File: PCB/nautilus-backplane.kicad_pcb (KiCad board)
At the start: 4 copper layers, 180 x 60 mm, 96 parts, among them J1 DE9_Socket_MountingHoles, J18 615008138321, J7 643280100305, J8 EdgeConn_Full, J9 643280100305

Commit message: Traced ethernet
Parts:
- moved TP1 50.8 mm to (269.5, 115.2)
- moved TP2 50.8 mm to (267.0, 115.2)
- moved JP15 41.6 mm to (173.6, 90.1)
- moved JP16 41.6 mm to (170.4, 90.1)
- moved JP17 41.6 mm to (173.6, 92.6)
- moved JP18 41.6 mm to (170.3, 92.6)
- moved JP27 41.6 mm to (162.8, 99.1)
- moved JP28 41.6 mm to (162.8, 94.1)
- moved JP29 41.6 mm to (162.8, 96.6)
- moved TP3 34.0 mm to (259.6, 110.7)
- moved J1 29.3 mm to (259.5, 77.2)
- moved J18 18.6 mm to (225.6, 102.5), turned to 90 degrees
- moved JP8 17.1 mm to (216.1, 110.6), turned to 0 degrees
- moved JP6 14.9 mm to (219.6, 109.4), turned to 0 degrees
- moved JP7 13.9 mm to (219.6, 111.9), turned to 0 degrees
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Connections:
- net /A16 renamed e1_3+
- net /A17 renamed e1_3-
- net /A18 renamed e1_2-
- net /A19 renamed e1_2+
- net /B12 renamed e2_1+
- net /B13 renamed e2_1-
- net /B14 renamed e2_0-
- net /B15 renamed e2_0+
- net /B16 renamed e1_1+
- net /B17 renamed e1_1-
- net /B18 renamed e1_0-
- net /B19 renamed e1_0+
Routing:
- net e1_0+: track 0.00 -> 64.8 mm
- net e1_0-: track 0.00 -> 64.5 mm
- net e1_1+: track 0.00 -> 63.1 mm
- net e1_1-: track 0.00 -> 63.1 mm
- net e1_2+: track 0.00 -> 59.2 mm
- net e1_2-: track 0.00 -> 59.0 mm
- net /TRD0.D+: track 22.6 -> 74.1 mm
- net /TRD0.D-: track 22.7 -> 74.1 mm
- net e1_3+: track 0.00 -> 48.0 mm
- net e1_3-: track 0.00 -> 47.7 mm
- net /TRD1.D+: track 22.6 -> 67.1 mm
- net /TRD1.D-: track 22.7 -> 67.1 mm
- net e2_0+: track 0.00 -> 24.4 mm
- net e2_0-: track 0.00 -> 24.4 mm
- net e2_1-: track 0.00 -> 20.6 mm
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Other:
- board text added: "24V"

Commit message: placed banana connectors for power
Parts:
- removed J7: 643280100305, dz_con:Wuerth_WR_CIRCM_643280100305
- added J2: 24.245.2, dz_con:ANT-TH_L33.0-W12.0, F.Cu at (118.5, 102.4)
- added J3: 24.245.2, dz_con:ANT-TH_L33.0-W12.0, F.Cu at (118.4, 122.0)
- added J4: 24.245.2, dz_con:ANT-TH_L33.0-W12.0, F.Cu at (118.5, 82.9)
- added J5: 24.245.2, dz_con:ANT-TH_L33.0-W12.0, F.Cu at (225.9, 80.7)
- moved TP1 152.4 mm to (117.1, 114.1), turned to -90 degrees
- moved TP2 151.3 mm to (117.1, 94.5), turned to -90 degrees
- moved J1 71.5 mm to (188.1, 81.4), turned to 180 degrees
- moved TP4 64.5 mm to (117.1, 74.9)
- moved TP3 40.6 mm to (233.7, 79.4)
- moved JP15 20.1 mm to (193.7, 90.8)
- moved JP16 20.1 mm to (190.5, 90.8)
- moved JP17 20.1 mm to (193.7, 93.3)
- moved JP18 20.1 mm to (190.4, 93.3)
- moved JP53 19.4 mm to (156.9, 104.8)
- moved JP54 19.4 mm to (156.9, 102.3)
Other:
- board size 180 x 60 mm -> 130.2 x 60.1 mm
- board text added: "3V3"
- board text added: "3v3"
- board text added: "5V"
- board text added: "GND"
- board text removed: "MB & CU"

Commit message: Traced CAN
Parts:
- JP15, JP16, JP17, JP18, JP27, JP28, JP29: moved to F.Cu
- JP35, JP36, JP50, JP51, JP52, R5, TP33, TP34: moved to B.Cu
- moved J9 225.1 mm to (163.9, 78.7), turned to 180 degrees
- moved JP50 146.3 mm to (192.8, 87.7), turned to 90 degrees
- moved TP33 146.2 mm to (206.5, 85.0), turned to -90 degrees
- moved TP34 146.0 mm to (206.5, 87.5), turned to -90 degrees
- moved JP52 145.2 mm to (190.3, 87.7), turned to 90 degrees
- moved R5 141.9 mm to (209.8, 87.6), turned to 180 degrees
- moved JP51 138.4 mm to (213.2, 85.0), turned to -90 degrees
- moved JP35 130.1 mm to (200.8, 87.7), turned to 90 degrees
- moved JP36 126.4 mm to (198.3, 87.7), turned to 90 degrees
- moved JP47 102.7 mm to (171.2, -25.7)
- moved JP48 102.7 mm to (171.2, -21.9)
- moved JP49 102.7 mm to (171.2, -18.1)
- moved JP43 102.7 mm to (165.9, -43.1)
- moved JP44 102.7 mm to (165.9, -39.3)
- moved JP45 102.7 mm to (165.9, -35.4)
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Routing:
- net /FISH/CAN.H: track 0.00 -> 88.5 mm, vias 0 -> 2
- net e2_1-: track 20.6 -> 107.0 mm, vias 0 -> 2
- net /FISH/CAN.L: track 0.00 -> 72.2 mm, vias 0 -> 2
- net /A13: track 0.00 -> 67.5 mm, vias 0 -> 1
- net /A12: track 0.00 -> 59.5 mm, vias 0 -> 2
- net e2_1+: track 20.6 -> 60.5 mm, vias 0 -> 2
- net /B31: track 0.00 -> 31.3 mm
- net /B32: track 0.00 -> 31.0 mm
- net Net-(JP51-B): track 0.00 -> 2.58 mm
- net e1_2+: track 59.2 -> 57.8 mm
- net e1_2-: track 59.0 -> 57.6 mm
- net e1_3+: track 48.0 -> 46.6 mm
- net e1_3-: track 47.7 -> 46.3 mm
- net GND: vias 0 -> 8
- net +5V: vias 0 -> 4
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- added copper zone on B.Cu, net +24V
- added copper zone on In2.Cu, net +24V
- added copper zone on F.Cu, net +3V3
- added copper zone on F.Cu, net +5V
- added copper zone on B.Cu, net /B45
- added copper zone on B.Cu, net /B48
- added copper zone on In2.Cu, net GND
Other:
- board text added: "BMS"
- board text added: "CAN Term"
- board text added: "CAN_H"
- board text added: "CAN_L"

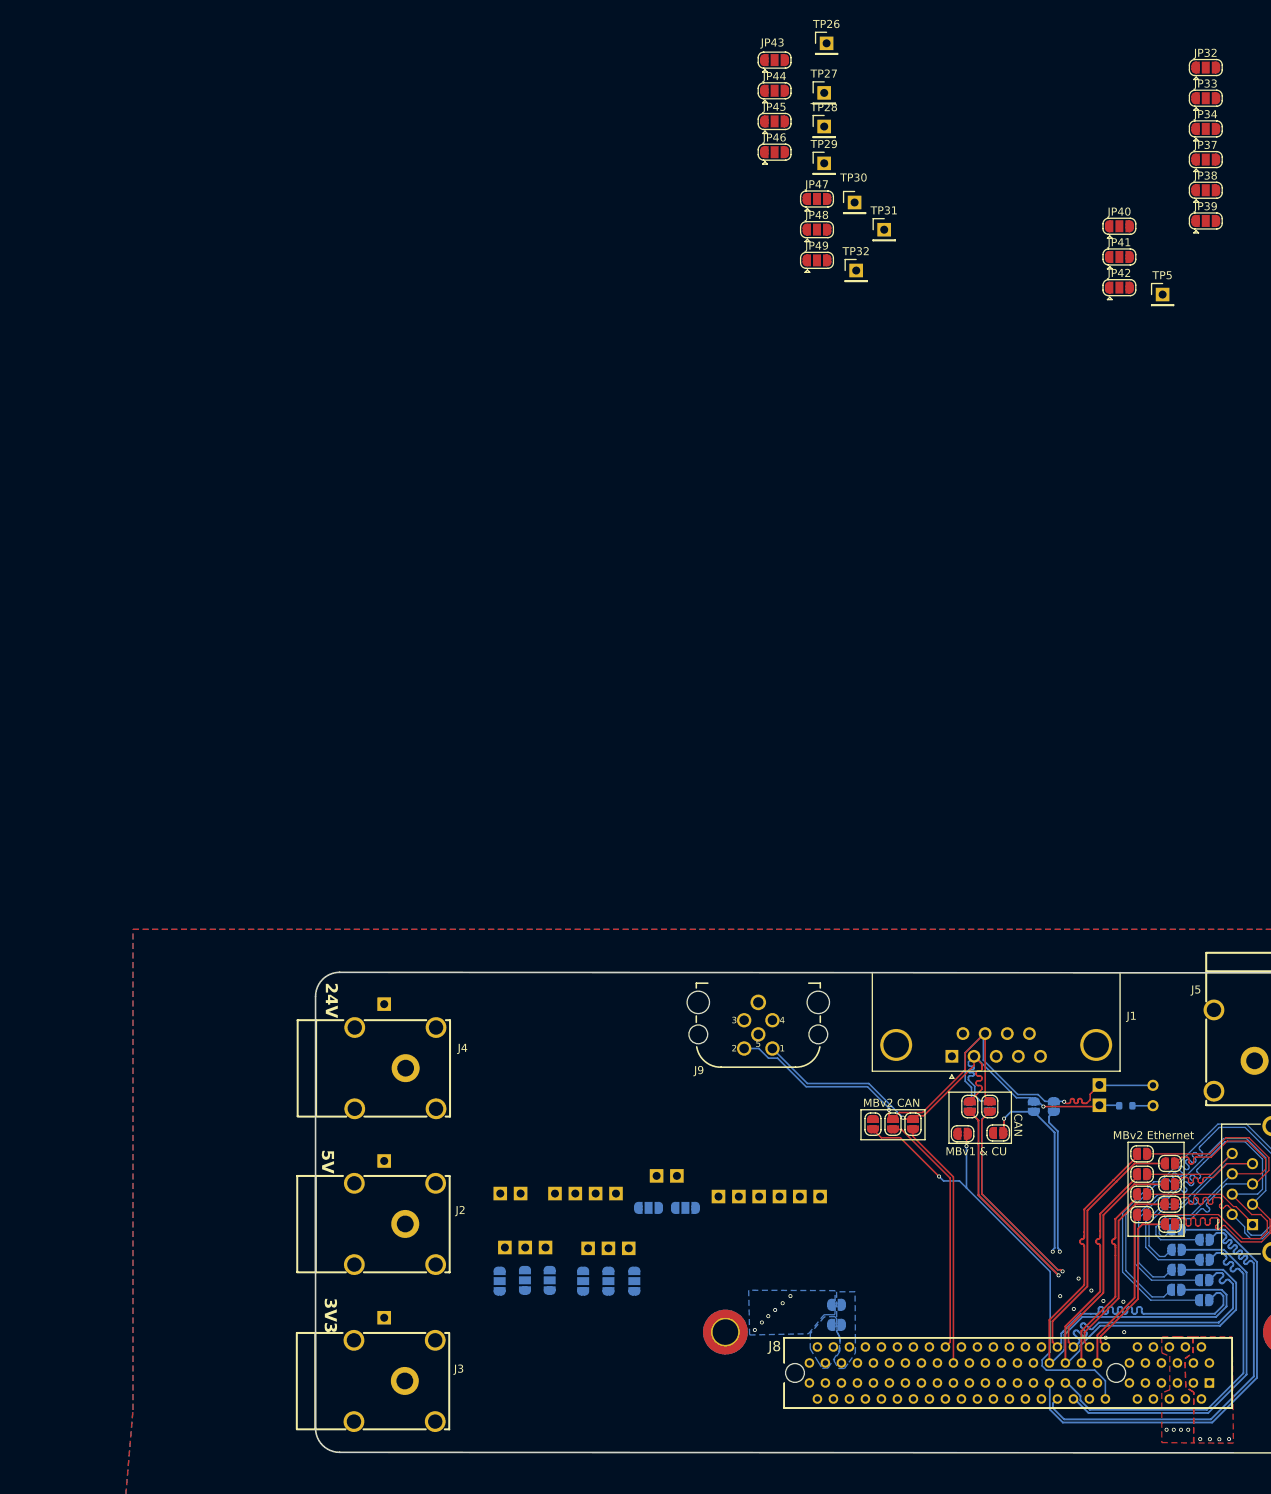
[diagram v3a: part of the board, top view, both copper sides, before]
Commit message: Traced around half of the board
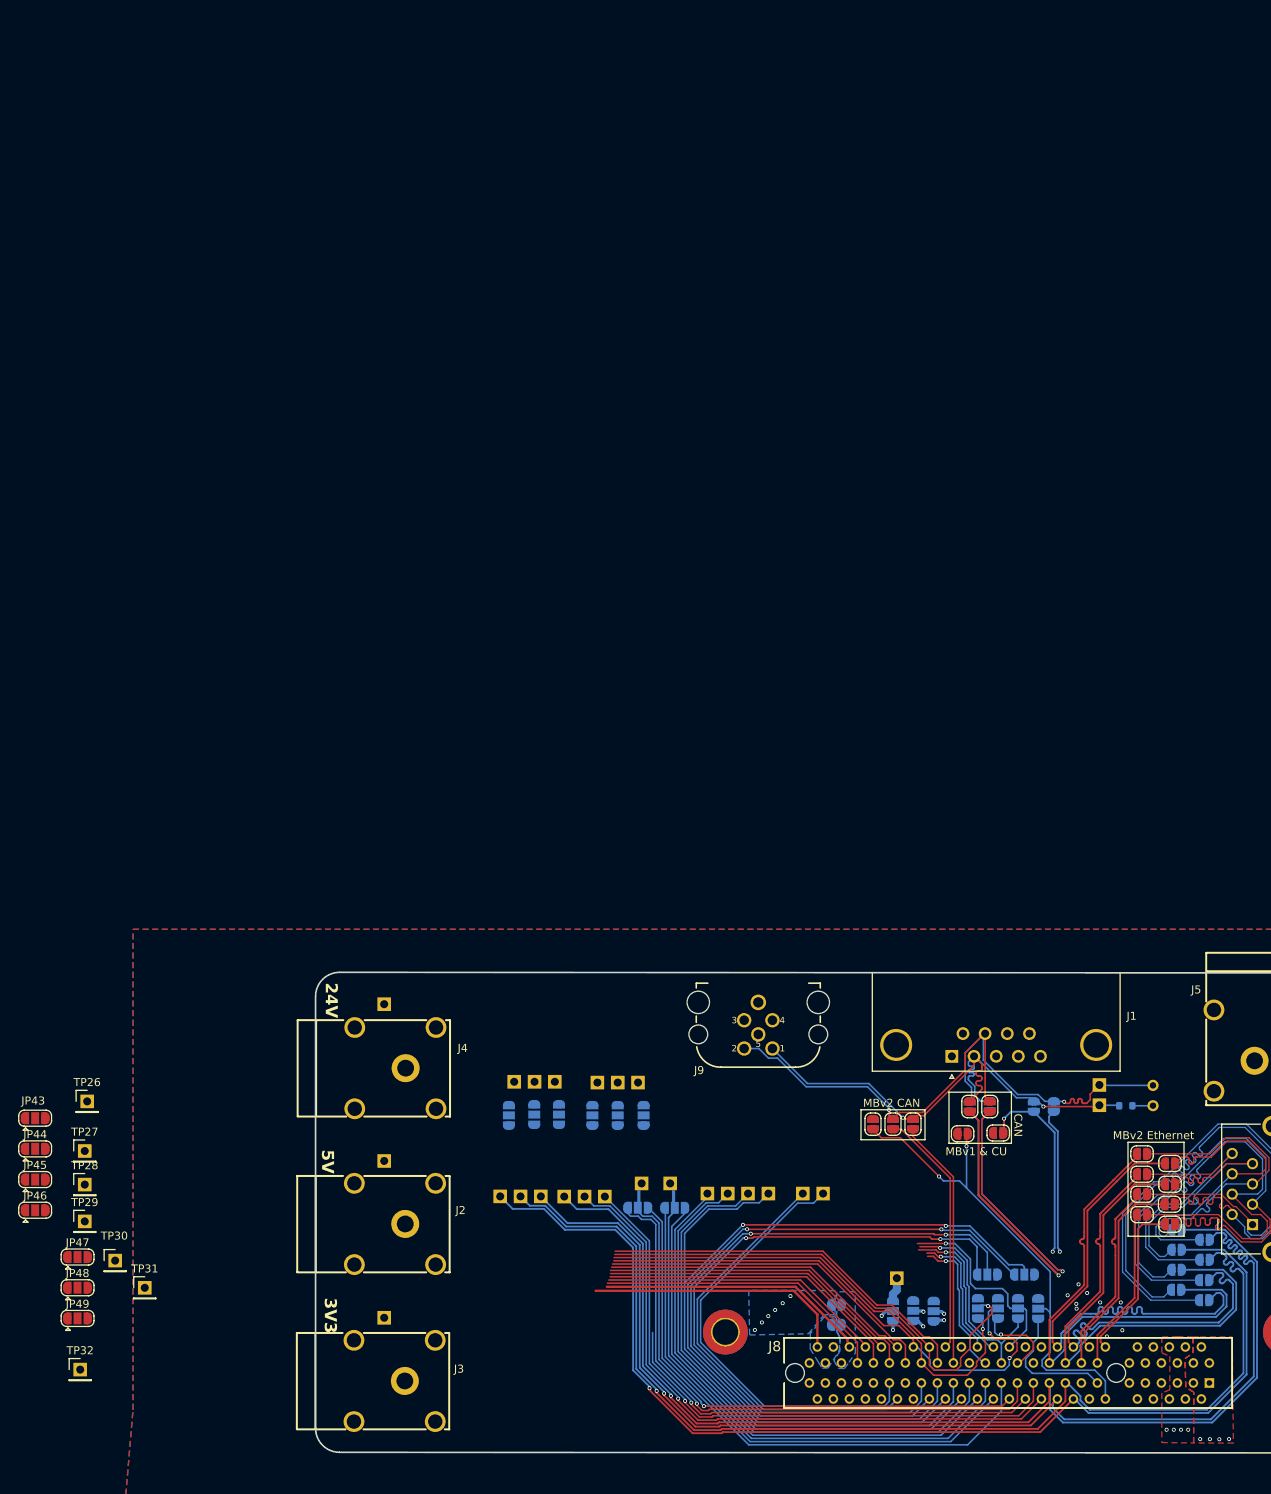
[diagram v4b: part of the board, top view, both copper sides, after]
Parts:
- JP32, JP33, JP34, JP37, JP38, JP39, JP40, JP41, JP42, TP5: moved to B.Cu
- moved TP32 168.2 mm to (79.1, 120.6)
- moved JP43 161.4 mm to (73.5, 89.2)
- moved JP44 161.4 mm to (73.5, 93.0)
- moved JP45 161.4 mm to (73.5, 96.8)
- moved JP46 161.4 mm to (73.5, 100.7)
- moved JP47 161.4 mm to (78.8, 106.5)
- moved JP48 161.4 mm to (78.8, 110.3)
- moved JP49 161.4 mm to (78.8, 114.2)
- moved TP26 161.4 mm to (80.0, 87.1)
- moved TP27 161.4 mm to (79.7, 93.3)
- moved TP28 161.4 mm to (79.7, 97.5)
- moved TP29 161.4 mm to (79.7, 102.1)
- moved TP30 161.4 mm to (83.5, 107.0)
- moved TP31 161.4 mm to (87.2, 110.4)
- moved JP32 156.5 mm to (198.8, 113.0), turned to -90 degrees
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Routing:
- net /A32: track 0.00 -> 113.2 mm, vias 0 -> 2
- net e1_3+: track 46.6 -> 141.5 mm, vias 0 -> 1
- net e1_3-: track 46.3 -> 139.6 mm, vias 0 -> 1
- net /A33: track 0.00 -> 92.0 mm, vias 0 -> 2
- net e1_2-: track 57.6 -> 144.8 mm, vias 0 -> 1
- net /A34: track 0.00 -> 85.3 mm, vias 0 -> 2
- net e1_2+: track 57.8 -> 142.8 mm, vias 0 -> 1
- net /A35: track 0.00 -> 84.0 mm, vias 0 -> 2
- net /A20: track 0.00 -> 79.0 mm, vias 0 -> 1
- net /A21: track 0.00 -> 77.3 mm, vias 0 -> 1
- net /A23: track 0.00 -> 72.6 mm, vias 0 -> 1
- net /A25: track 0.00 -> 71.7 mm
- net /A24: track 0.00 -> 70.7 mm, vias 0 -> 1
- net /A27: track 0.00 -> 70.2 mm
- net /B36: track 0.00 -> 68.0 mm, vias 0 -> 2
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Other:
- board text added: "VBAT out"

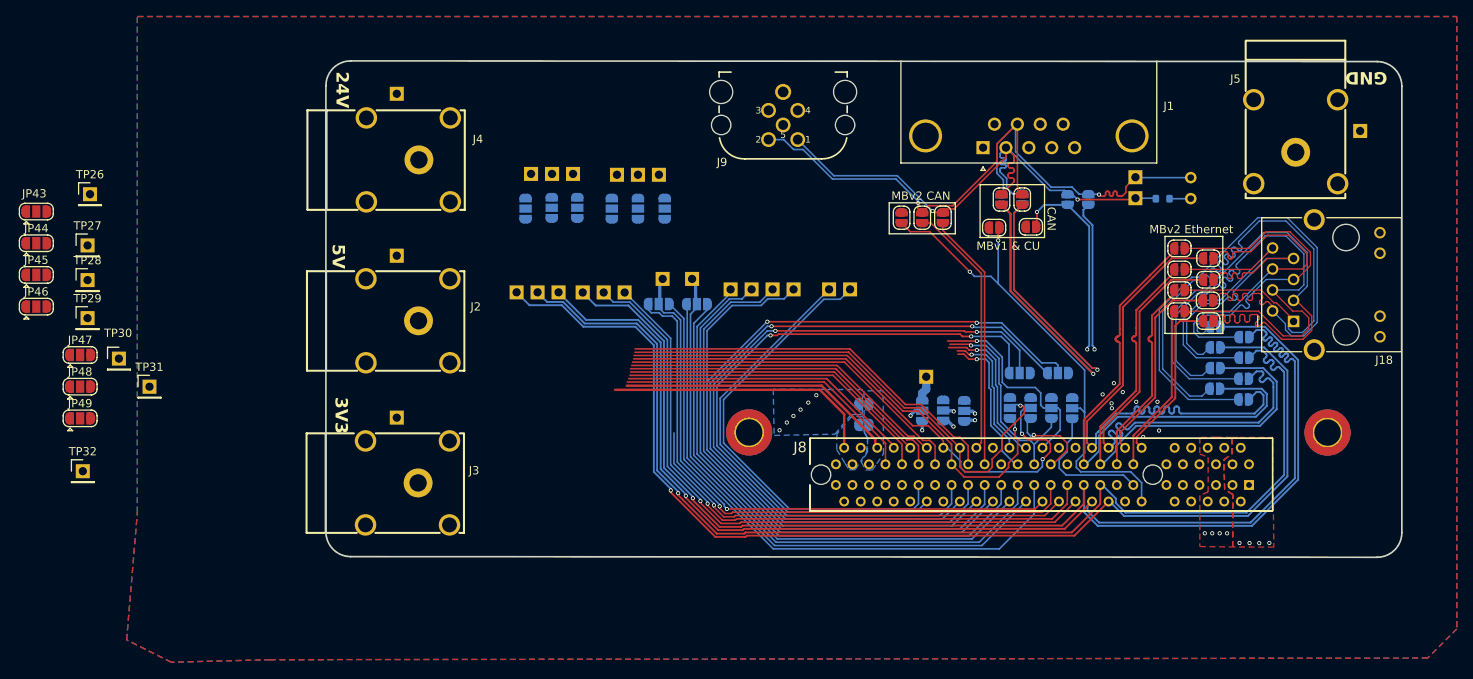
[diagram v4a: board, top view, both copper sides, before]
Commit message: Traced everything; TODO: tune trace length, fix drc error
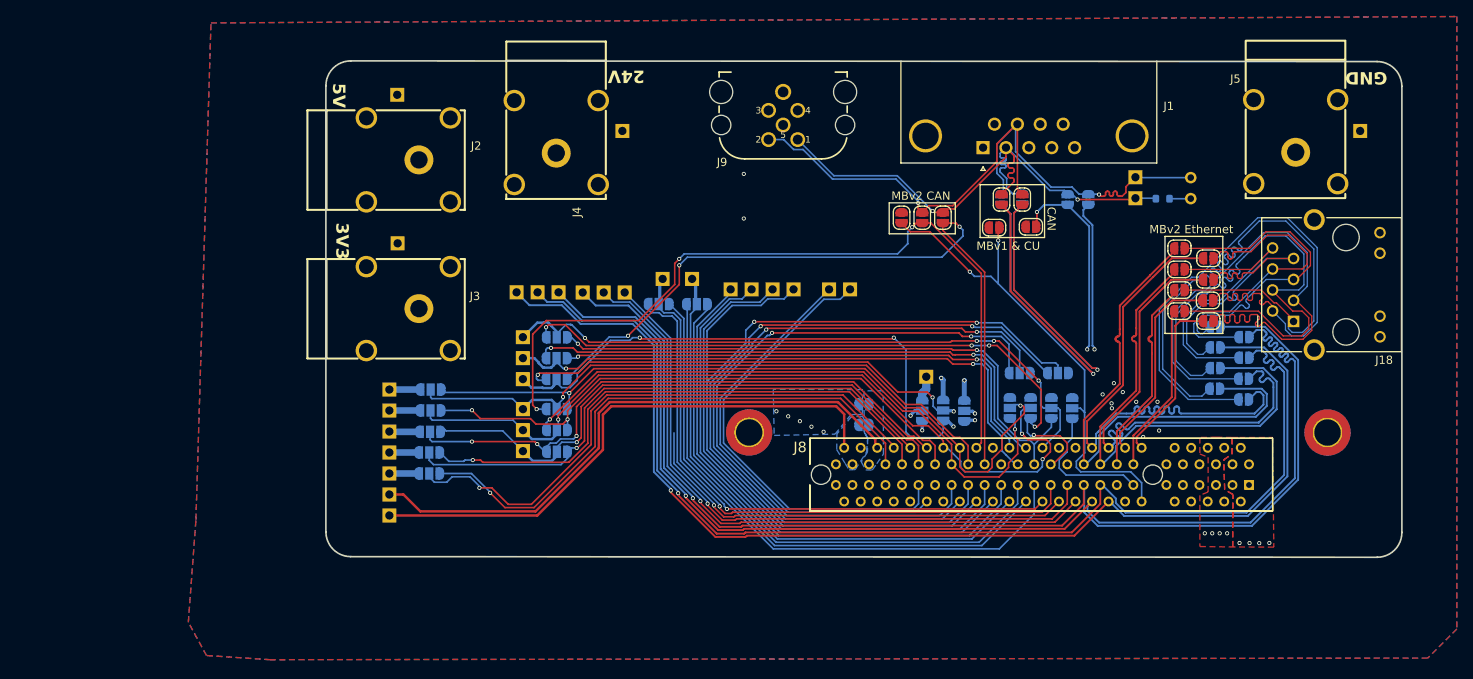
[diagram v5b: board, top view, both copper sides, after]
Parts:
- removed JP48, JP49: SolderJumper_3_Open, Jumper:SolderJumper-3_P1.3mm_Open_RoundedPad1.0x1.5mm
- JP43, JP44, JP45, JP46, JP47, TP26, TP27, TP28, TP29, TP30, TP31, TP32: moved to B.Cu
- moved JP43 52.4 mm to (121.2, 110.7)
- moved JP44 51.8 mm to (121.2, 113.2)
- moved JP45 51.3 mm to (121.1, 115.8)
- moved JP46 50.7 mm to (121.0, 118.3)
- moved JP47 44.6 mm to (121.0, 120.9)
- moved TP26 43.3 mm to (116.2, 110.7), turned to 90 degrees
- moved TP27 41.6 mm to (116.2, 113.2), turned to 90 degrees
- moved TP28 40.9 mm to (116.2, 115.8), turned to 90 degrees
- moved TP29 40.0 mm to (116.2, 118.3), turned to 90 degrees
- moved TP32 37.5 mm to (116.2, 125.9), turned to 90 degrees
- moved TP30 35.6 mm to (116.2, 120.9), turned to 90 degrees
- moved TP9 33.6 mm to (132.4, 118.2), turned to -90 degrees
- moved TP31 31.8 mm to (116.2, 123.4), turned to 90 degrees
- moved TP10 31.2 mm to (132.4, 115.6), turned to -90 degrees
- moved JP12 29.7 mm to (136.5, 118.2), turned to 0 degrees
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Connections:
- TP31 pad 1: /BAT_P5 -> /B45
- TP32 pad 1: /BAT_P6 -> /B48
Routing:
- net +3V3: track 0.00 -> 117.4 mm, vias 4 -> 5
- net +5V: track 0.00 -> 89.4 mm, vias 4 -> 5
- net /B23: track 10.9 -> 81.5 mm, vias 1 -> 5
- net /B30: track 7.79 -> 75.7 mm, vias 1 -> 3
- net /B32: track 31.0 -> 96.5 mm, vias 0 -> 3
- net /B31: track 31.3 -> 91.2 mm, vias 0 -> 3
- net /B29: track 11.2 -> 65.8 mm, vias 1 -> 3
- net /B27: track 18.1 -> 72.5 mm, vias 1 -> 2
- net /B24: track 25.2 -> 79.4 mm, vias 1 -> 4
- net /B26: track 18.7 -> 68.0 mm, vias 1 -> 2
- net /B28: track 16.1 -> 62.6 mm, vias 1 -> 2
- net /B25: track 25.9 -> 72.0 mm, vias 1 -> 2
- net /B45: track 33.9 -> 70.6 mm
- net /B48: track 33.0 -> 67.5 mm
- net /B42: track 35.7 -> 69.3 mm, vias 0 -> 1
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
